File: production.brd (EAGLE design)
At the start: 118 x 173.7 mm, 60 parts, among them CN1 1X4-3.5MM, CN2 1X4-3.5MM, CN3 1X4-3.5MM, IC1 3v3, IC2 5v, IC3 3v3, IC4 5v, IC5 3v3, IC6 5v, M1 ARDUINO-NANO-3.0#ISP, M2 ARDUINO-NANO-3.0#ISP, M3 ARDUINO-NANO-3.0#ISP

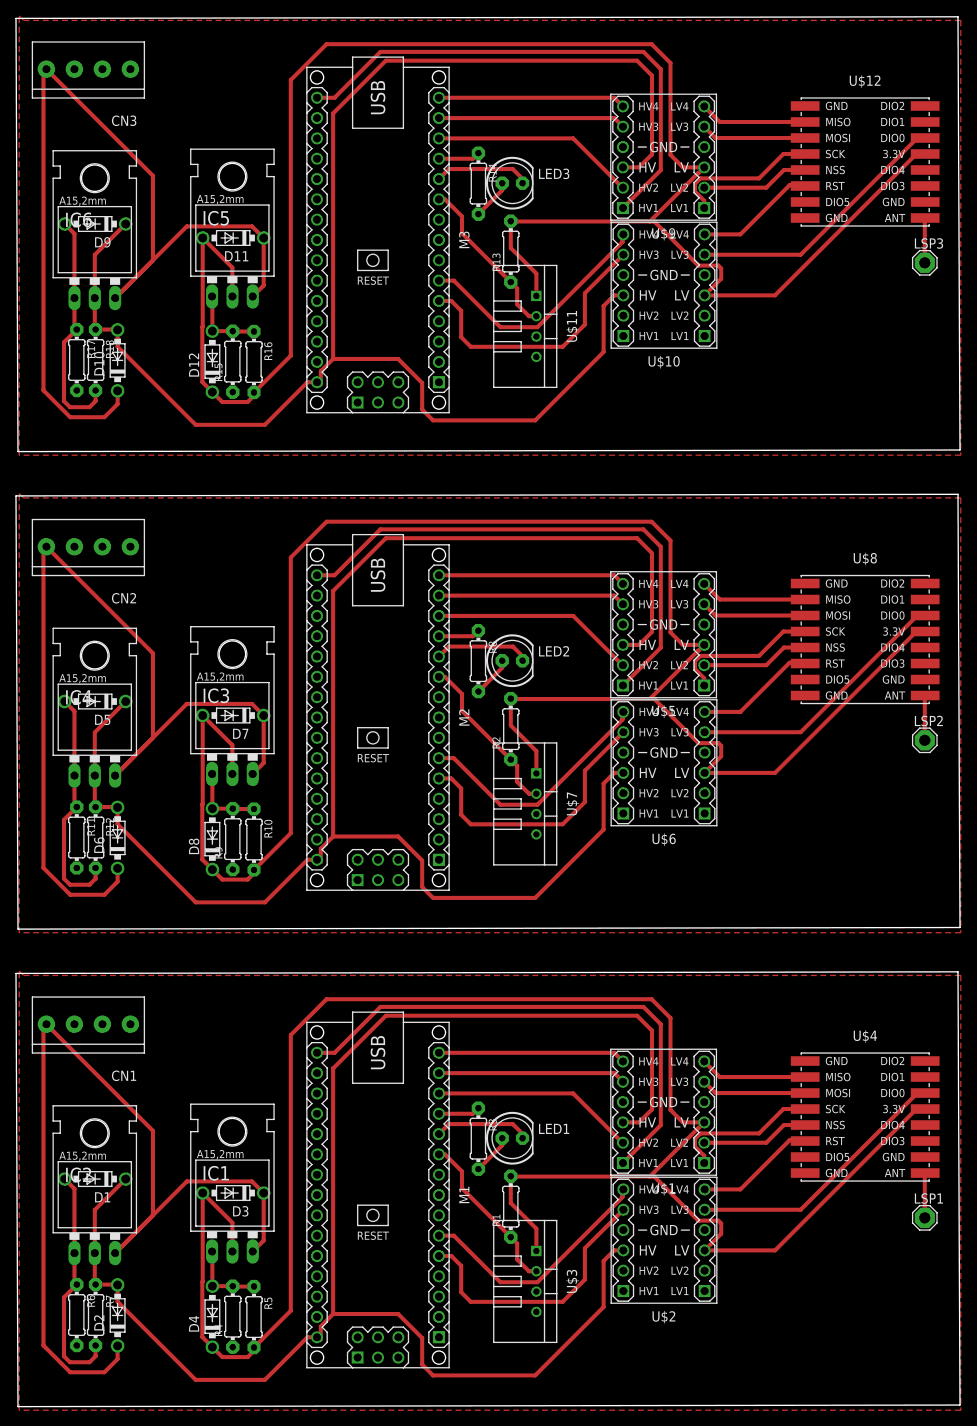
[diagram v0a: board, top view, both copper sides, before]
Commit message: Add production schematics.
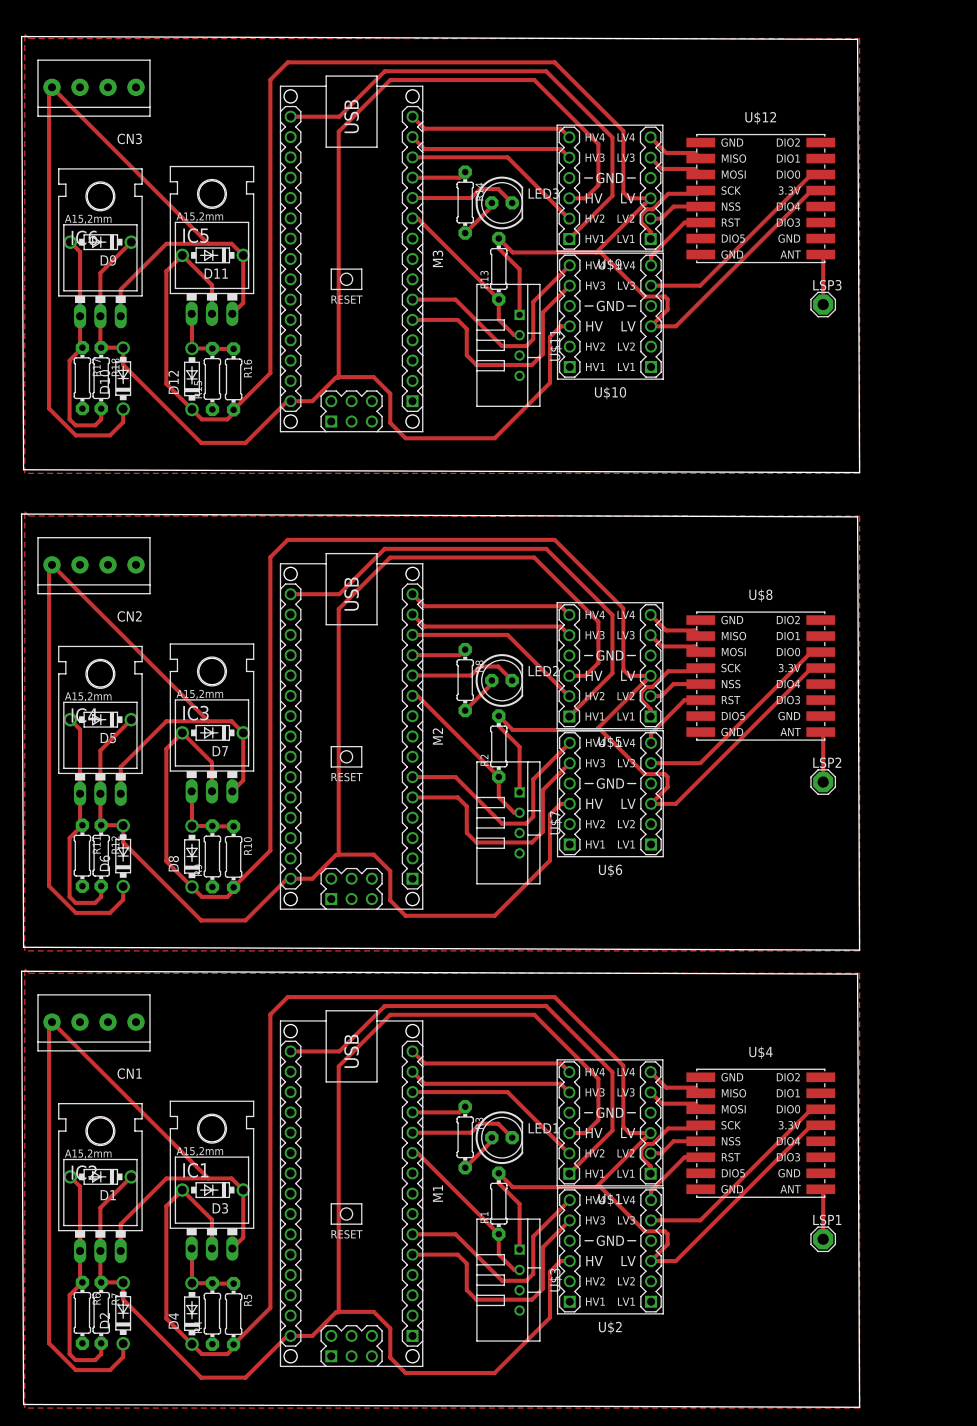
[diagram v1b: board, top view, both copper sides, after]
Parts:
- moved U$12 13.8 mm to (92.7, 151.3)
- moved U$8 13.8 mm to (92.7, 91.6)
- moved LSP2 13.7 mm to (100.5, 78.3)
- moved LSP3 13.7 mm to (100.5, 138.0)
- moved U$4 13.2 mm to (92.7, 34.4)
- moved LSP1 13.0 mm to (100.5, 21.2)
- moved U$9 7.74 mm to (73.8, 152.6)
- moved U$5 7.74 mm to (73.8, 92.9)
- moved U$10 7.74 mm to (73.9, 136.6)
- moved U$6 7.74 mm to (73.9, 76.9)
- moved U$1 6.83 mm to (73.8, 35.7)
- moved U$2 6.83 mm to (73.9, 19.7)
- moved M2 4.06 mm to (41.5, 84.0)
- moved M3 4.06 mm to (41.5, 143.7)
- moved IC5 3.35 mm to (24.1, 140.7)
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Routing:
- net 5.1V: track 195.4 -> 176.2 mm
- net 5.1V2: track 195.4 -> 176.2 mm
- net 5.1V1: track 195.4 -> 176.2 mm
- net 3V3.1: track 230.9 -> 216.8 mm
- net 3V3.3: track 230.9 -> 216.8 mm
- net 3V3.2: track 230.9 -> 216.8 mm
- net 9V2: track 120.1 -> 110.5 mm
- net 9V: track 120.1 -> 110.5 mm
- net 9V1: track 120.1 -> 110.5 mm
- net N$44: track 16.5 -> 9.11 mm
- net N$17: track 16.5 -> 9.11 mm
- net N$29: track 16.5 -> 9.11 mm
- net N$42: track 13.5 -> 6.90 mm
- net N$27: track 13.5 -> 6.90 mm
- net INT2: track 33.6 -> 27.0 mm
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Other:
- board size 118 x 173.7 mm -> 104.8 x 171.3 mm

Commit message: Add arduino pro mini 5v.
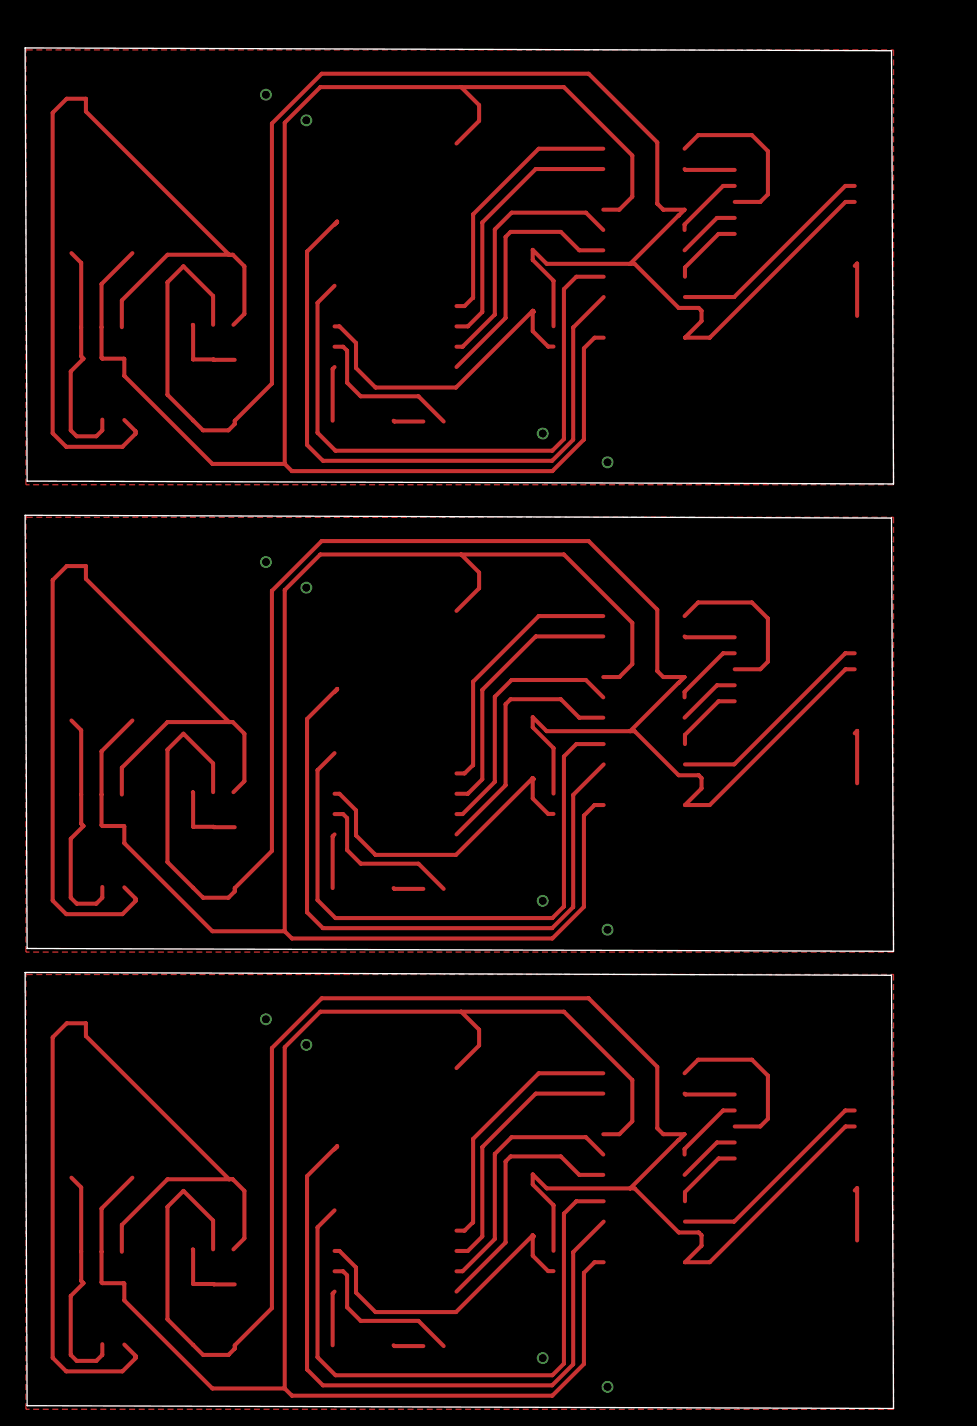
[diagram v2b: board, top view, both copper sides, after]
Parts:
- removed CN1, CN2, CN3: 1X4-3.5MM, adafruit:1X04-3.5MM
- removed D1, D10, D11, D12, D2, D3, D4, D5, D6, D7, D8, D9: 1N5817-B, diode:DO41-7.6
- removed IC1, IC3, IC5: 3v3, v-reg:317TL
- removed IC2, IC4, IC6: 5v, v-reg:317TL
- removed LED1, LED2, LED3: (no value), adafruit:LED5MM
- removed LSP1, LSP2, LSP3: SE14, solpad:SE14
- removed M1, M2, M3: ARDUINO-NANO-3.0#ISP, dht22:ARDUINO-NANO-3.0#ISP
- removed R1, R13, R2: 10k, adafruit:0204/7
- removed R10, R16, R5: 4.7k, adafruit:0204/7
- removed R11, R17, R6: 1.5k, adafruit:0204/7
- removed R12, R18, R7: (no value), adafruit:0204/7
- removed R14, R3, R8: 220, adafruit:0204/7
- removed R15, R4, R9: 2.7k, adafruit:0204/7
- removed U$1, U$10, U$2, U$5, U$6, U$9: LEVEL-SHIFTER-4CH, dht22:LEVEL-SHIFTER-4CH
- removed U$11, U$3, U$7: TEMP-HUM-SENSOR-DHT22, dht22:TEMP-HUM-SENSOR-DHT22
- removed U$12, U$4, U$8: WIRELESS-LORA-RFM95W#SMD, dht22:WIRELESS-LORA-RFM95W#SMD
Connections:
- removed net 3V3.1: D3.A, D4.C, IC1.2, M1.J2.14, R1.2, R5.2, U$1.J1.3, U$2.J1.3, U$3.1, U$4.B4
- removed net 3V3.2: D7.A, D8.C, IC3.2, M2.J2.14, R10.2, R2.2, U$5.J1.3, U$6.J1.3, U$7.1, U$8.B4
- removed net 3V3.3: D11.A, D12.C, IC5.2, M3.J2.14, R13.2, R16.2, U$10.J1.3, U$11.1, U$12.B4, U$9.J1.3
- removed net 5.1V: D1.C, D2.A, IC2.2, M1.J2.1, M1.J2.4, R7.1, U$1.J2.3, U$2.J2.3
- removed net 5.1V1: D5.C, D6.A, IC4.2, M2.J2.1, M2.J2.4, R12.1, U$5.J2.3, U$6.J2.3
- removed net 5.1V2: D10.A, D9.C, IC6.2, M3.J2.1, M3.J2.4, R18.1, U$10.J2.3, U$9.J2.3
- removed net 9V: CN1.1, D2.C, D3.C, IC1.3, IC2.3
- removed net 9V1: CN2.1, D6.C, D7.C, IC3.3, IC4.3
- removed net 9V2: CN3.1, D10.C, D11.C, IC5.3, IC6.3
- removed net D1: M2.J1.10, R2.1, U$7.2
- removed net D2: M3.J1.10, R13.1, U$11.2
- removed net D7: M1.J1.10, R1.1, U$3.2
- removed net GND: CN1.2, M1.J1.4, M1.J2.2, R4.1, R6.2, U$1.J1.4, U$1.J2.4, U$2.J1.4, U$2.J2.4, U$3.4, U$4.A1, U$4.A8, U$4.B7
- removed net GND1: CN2.2, M2.J1.4, M2.J2.2, R11.2, R9.1, U$5.J1.4, U$5.J2.4, U$6.J1.4, U$6.J2.4, U$7.4, U$8.A1, U$8.A8, U$8.B7
- removed net GND2: CN3.2, M3.J1.4, M3.J2.2, R15.1, R17.2, U$10.J1.4, U$10.J2.4, U$11.4, U$12.A1, U$12.A8, U$12.B7, U$9.J1.4, U$9.J2.4
- removed net INT: U$2.J1.5, U$4.B3
- removed net INT1: U$6.J1.5, U$8.B3
- removed net INT2: U$10.J1.5, U$12.B3
- removed net LED+: M1.J1.12, R3.1
- removed net LED+1: M2.J1.12, R8.1
- removed net LED+2: M3.J1.12, R14.1
- removed net LEDGND: LED1.K, M1.J1.11
- removed net LEDGND1: LED2.K, M2.J1.11
- removed net LEDGND2: LED3.K, M3.J1.11
- removed net N$1: D4.A, IC1.1, R4.2, R5.1
- removed net N$10: LSP1.MP, U$4.B8
- removed net N$11: D8.A, IC3.1, R10.1, R9.2
- removed net N$12: D5.A, IC4.1, R11.1, R12.2
- removed net N$13: U$1.J1.6, U$4.A2
- removed net N$14: U$1.J1.5, U$4.A3
- removed net N$15: U$1.J1.2, U$4.A5
- removed net N$16: U$1.J1.1, U$4.A4
- removed net N$17: U$2.J1.6, U$4.A6
- removed net N$18: LED2.A, R8.2
- removed net N$19: M2.J1.5, U$6.J2.5
- removed net N$2: LED1.A, R3.2
- removed net N$20: M2.J1.6, U$6.J2.6
- removed net N$21: M2.J2.15, U$5.J2.1
- removed net N$22: M2.J1.15, U$5.J2.6
- removed net N$23: M2.J1.14, U$5.J2.5
- removed net N$24: M2.J1.13, U$5.J2.2
- removed net N$25: U$5.J1.6, U$8.A2
- removed net N$26: U$5.J1.5, U$8.A3
- removed net N$27: U$5.J1.2, U$8.A5
- removed net N$28: U$5.J1.1, U$8.A4
- removed net N$29: U$6.J1.6, U$8.A6
- removed net N$3: M1.J2.15, U$1.J2.1
- removed net N$30: LSP2.MP, U$8.B8
- removed net N$31: D12.A, IC5.1, R15.2, R16.1
- removed net N$32: D9.A, IC6.1, R17.1, R18.2
- removed net N$33: LED3.A, R14.2
- removed net N$34: M3.J1.5, U$10.J2.5
- removed net N$35: M3.J1.6, U$10.J2.6
- removed net N$36: M3.J2.15, U$9.J2.1
- removed net N$37: M3.J1.15, U$9.J2.6
- removed net N$38: M3.J1.14, U$9.J2.5
- removed net N$39: M3.J1.13, U$9.J2.2
- removed net N$4: M1.J1.5, U$2.J2.5
- removed net N$40: U$12.A2, U$9.J1.6
- removed net N$41: U$12.A3, U$9.J1.5
- removed net N$42: U$12.A5, U$9.J1.2
- removed net N$43: U$12.A4, U$9.J1.1
- removed net N$44: U$10.J1.6, U$12.A6
- removed net N$45: LSP3.MP, U$12.B8
- removed net N$5: D1.A, IC2.1, R6.1, R7.2
- removed net N$6: M1.J1.6, U$2.J2.6
- removed net N$7: M1.J1.15, U$1.J2.6
- removed net N$8: M1.J1.14, U$1.J2.5
- removed net N$9: M1.J1.13, U$1.J2.2
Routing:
- net N$26: track 7.14 -> 84.6 mm
- net N$41: track 7.14 -> 84.6 mm
- net N$40: track 7.37 -> 75.9 mm
- net N$25: track 7.37 -> 75.9 mm
- net N$9: track 22.8 -> 84.6 mm
- net N$8: track 20.7 -> 75.9 mm
- net N$21: track 61.0 -> 6.97 mm
- net N$36: track 61.0 -> 6.97 mm
- net 5.1V2: track 176.2 -> 208.2 mm
- net 5.1V: track 176.2 -> 208.2 mm
- net 5.1V1: track 176.2 -> 208.2 mm
- net N$3: track 61.0 -> 33.0 mm
- net N$45: track 6.97 -> 32.6 mm
- net N$30: track 6.97 -> 32.6 mm
- net N$14: track 7.14 -> 32.6 mm
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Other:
- board size 104.8 x 171.3 mm -> 108.6 x 170.1 mm
